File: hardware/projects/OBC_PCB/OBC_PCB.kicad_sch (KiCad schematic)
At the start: 40 parts, among them U6 nRF54LM20A-QGAA, Y1 32MHz, Y3 32.768kHz

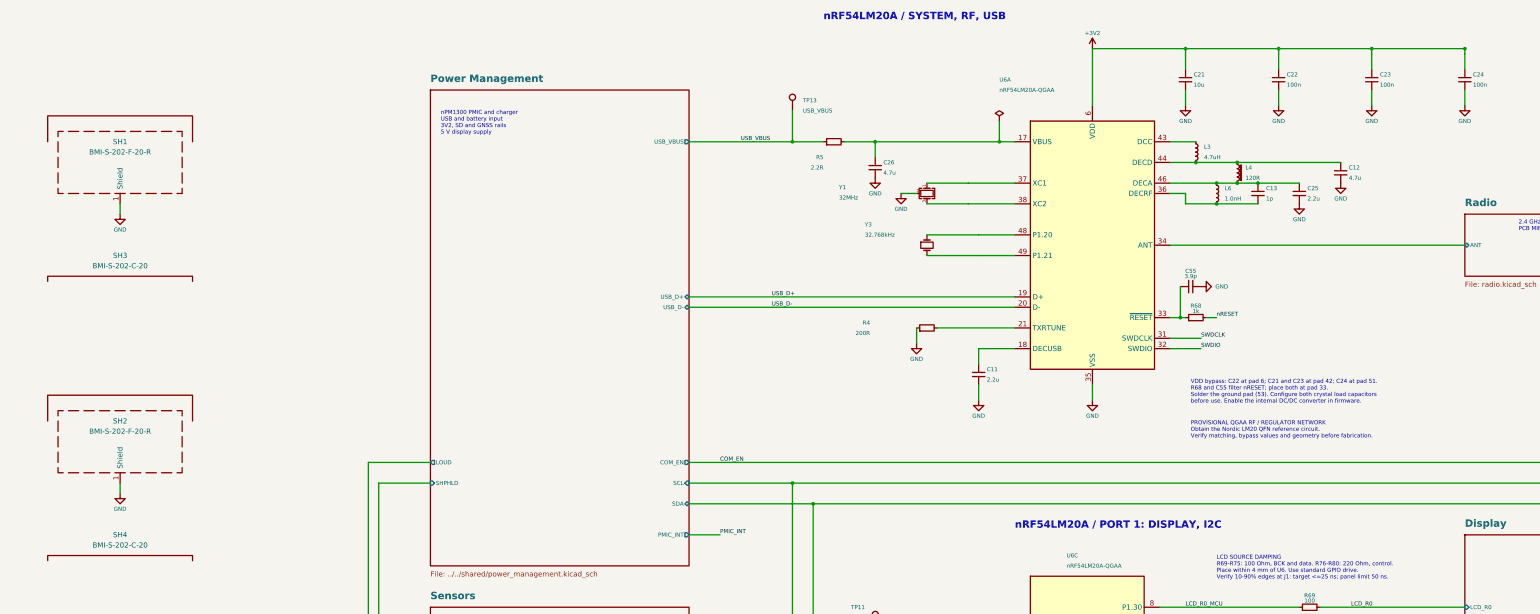
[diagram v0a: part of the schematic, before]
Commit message: hardware: save current KiCad schematic and project files
Retain the saved KiCad 10 schematic files and project sheet list.
The native netlist matches the committed placement circuit: 172
components and 140 nets. Public docs unchanged.
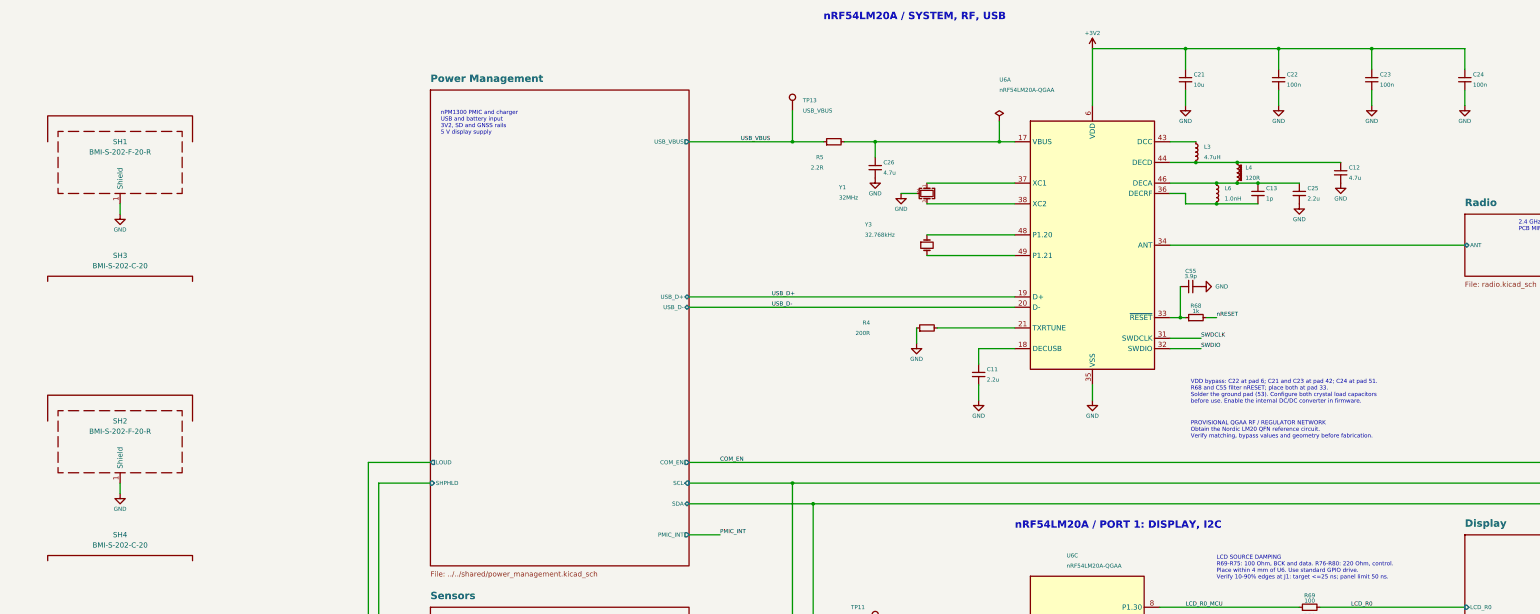
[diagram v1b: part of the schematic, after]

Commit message: hardware: add editable KiCad BOM and schematic exports
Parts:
- C11: DigiKey (none) -> https://www.digikey.de/en/products/detail/samsung-electro-m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; MPN (none) -> CL05A225KP5NNNC; Manufacturer (none) -> Samsung Electro-Mechanics; Mouser (none) -> https://www.mouser.com/en/ProductDetail/Samsung-Electro-Mec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; Price breaks EUR (none) -> 1:0.12000;10:0.06700;50:0.04740;100:0.04110;500:0.03058;100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; Price checked (none) -> 2026-10-02; Price source (none) -> https://www.digikey.de/en/products/detail/samsung-electro-m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; Sourcing notes (none) -> Mouser shows limited stock; DigiKey EUR price used.
- C12: Mouser (none) -> https://eu.mouser.com/en/ProductDetail/Murata-Electronics/G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; Price breaks EUR (none) -> 1:0.206;10:0.127;100:0.077;500:0.06;1000:0.054;2500:0.048;5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; Price checked (none) -> 2026-10-02; Price source (none) -> https://eu.mouser.com/en/ProductDetail/Murata-Electronics/G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
- C13: Mouser (none) -> https://eu.mouser.com/en/ProductDetail/Murata-Electronics/G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; Price breaks EUR (none) -> 1:0.086;10:0.034;100:0.028;500:0.022;1000:0.019;2500:0.017;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; Price checked (none) -> 2026-10-02; Price source (none) -> https://eu.mouser.com/en/ProductDetail/Murata-Electronics/G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
- C21: MPN (none) -> CC0402MRX6S5BB106; Manufacturer (none) -> YAGEO; Mouser (none) -> https://www.mouser.es/es/ProductDetail/YAGEO/CC0402MRX6S5BB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; Price breaks EUR (none) -> 1:0.542;10:0.294;100:0.217;500:0.174; Price checked (none) -> 2026-10-02; Price source (none) -> https://www.mouser.es/es/ProductDetail/YAGEO/CC0402MRX6S5BB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
- C22, C23, C24: DigiKey (none) -> https://www.digikey.de/en/products/detail/murata-electronic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; MPN (none) -> GRM155R71A104KA01D; Manufacturer (none) -> Murata; Price breaks EUR (none) -> 1:0.09000;10:0.02100;50:0.01400;100:0.01190;500:0.00830; Price checked (none) -> 2026-10-02; Price source (none) -> https://www.digikey.de/en/products/detail/murata-electronic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
- C25: Mouser (none) -> https://hr.mouser.com/en/ProductDetail/Murata-Electronics/G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; Price breaks EUR (none) -> 1:0.103;10:0.04;100:0.035;500:0.026;1000:0.024;2500:0.022;5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; Price checked (none) -> 2026-10-02; Price source (none) -> https://hr.mouser.com/en/ProductDetail/Murata-Electronics/G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
- C26: Mouser (none) -> https://gr.mouser.com/en/ProductDetail/Murata-Electronics/G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; Price breaks EUR (none) -> 1:0.146;10:0.061;100:0.035;500:0.028;1000:0.022;2500:0.02;5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; Price checked (none) -> 2026-10-02; Price source (none) -> https://gr.mouser.com/en/ProductDetail/Murata-Electronics/G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
- C55: MPN (none) -> GJM0335C1E3R9BB01D; Manufacturer (none) -> Murata; Mouser (none) -> https://www.mouser.fr/ProductDetail/Murata-Electronics/GJM0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; Price breaks EUR (none) -> 1:0.086;10:0.023;100:0.021;500:0.015; Price checked (none) -> 2026-10-02; Price source (none) -> https://www.mouser.fr/ProductDetail/Murata-Electronics/GJM0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
- L3: DigiKey (none) -> https://www.digikey.de/en/products/detail/tdk/MLZ1608M4R7WT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; Mouser (none) -> https://eu.mouser.com/en/ProductDetail/TDK/MLZ1608M4R7WT000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; Price breaks EUR (none) -> 1:0.09000;10:0.07400;100:0.06040;1000:0.04959; Price checked (none) -> 2026-10-02; Price source (none) -> https://www.digikey.de/en/products/detail/tdk/MLZ1608M4R7WT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
- L4: Mouser (none) -> https://www.mouser.sk/en/ProductDetail/Murata-Electronics/B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; Price breaks EUR (none) -> 1:0.086;10:0.022;25:0.018;100:0.015;250:0.014;500:0.012;100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; Price checked (none) -> 2026-10-02; Price source (none) -> https://www.mouser.sk/en/ProductDetail/Murata-Electronics/B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
- L6: Mouser (none) -> https://www.mouser.es/ProductDetail/Murata-Electronics/LQP0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; Price breaks EUR (none) -> 1:0.086;10:0.022;100:0.018;1000:0.015;5000:0.011; Price checked (none) -> 2026-10-02; Price source (none) -> https://www.mouser.es/ProductDetail/Murata-Electronics/LQP0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
- R4: MPN (none) -> RC0402FR-07200RL; Manufacturer (none) -> YAGEO; Mouser (none) -> https://www.mouser.de/de/ProductDetail/YAGEO/RC0402FR-07200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; Power 63mW -> 62.5mW; Price breaks EUR (none) -> 1:0.086;10:0.008;100:0.005;2500:0.003; Price checked (none) -> 2026-10-02; Price source (none) -> https://www.mouser.de/de/ProductDetail/YAGEO/RC0402FR-07200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
- R5: DigiKey (none) -> https://www.digikey.fr/fr/products/detail/yageo/RC0402FR-07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; MPN (none) -> RC0402FR-072R2L; Manufacturer (none) -> YAGEO; Mouser (none) -> https://www.mouser.com/en/ProductDetail/YAGEO/RC0402FR-072R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; Power 63mW -> 62.5mW; Price breaks EUR (none) -> 1:0.09;10:0.021;25:0.0152;50:0.0122;100:0.0099;250:0.0076;5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; Price checked (none) -> 2026-10-02; Price source (none) -> https://www.digikey.fr/fr/products/detail/yageo/RC0402FR-07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; Technology (none) -> Thick film
- R68: DigiKey (none) -> https://www.digikey.de/de/products/detail/yageo/RC0201FR-07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; MPN (none) -> RC0201FR-071KL; Manufacturer (none) -> YAGEO; Mouser (none) -> https://gr.mouser.com/en/ProductDetail/YAGEO/RC0201FR-071KL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; Power 63mW -> 50mW; Price breaks EUR (none) -> 1:0.172;10:0.017;100:0.011;1000:0.009; Price checked (none) -> 2026-10-02; Price source (none) -> https://gr.mouser.com/en/ProductDetail/YAGEO/RC0201FR-071KL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; Selection notes (none) -> Candidate; verify the 0201 part rating of 50mW/25V against 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; Voltage 50V -> 25V
- R69, R70, R71, R72, R73, R74, R75: Mouser (none) -> https://eu.mouser.com/ProductDetail/YAGEO/RC0201FR-07100RL?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; Price breaks EUR (none) -> 1:0.086;10:0.008;100:0.006;1000:0.005; Price checked (none) -> 2026-10-02; Price source (none) -> https://eu.mouser.com/ProductDetail/YAGEO/RC0201FR-07100RL?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
- R76, R77, R78, R79, R80: Mouser (none) -> https://eu.mouser.com/en/ProductDetail/YAGEO/RC0201FR-07220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; Price breaks EUR (none) -> 1:0.086;10:0.009;100:0.007;1000:0.005; Price checked (none) -> 2026-10-02; Price source (none) -> https://eu.mouser.com/en/ProductDetail/YAGEO/RC0201FR-07220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
- R9: MPN (none) -> RC0402FR-0733RL; Manufacturer (none) -> YAGEO; Mouser (none) -> https://eu.mouser.com/en/ProductDetail/YAGEO/RC0402FR-0733R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; Power 63mW -> 62.5mW; Price breaks EUR (none) -> 1:0.086;10:0.009;100:0.006;1000:0.005;2500:0.003; Price checked (none) -> 2026-10-02; Price source (none) -> https://eu.mouser.com/en/ProductDetail/YAGEO/RC0402FR-0733R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
- SH1, SH2: DigiKey (none) -> https://www.digikey.ie/en/products/detail/laird-technologie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; Price breaks EUR (none) -> 1:1.70000;10:1.46300;25:1.38160;100:1.26850;250:1.20076; Price checked (none) -> 2026-10-02; Price source (none) -> https://www.digikey.ie/en/products/detail/laird-technologie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
- SH3, SH4: Mouser (none) -> https://eu.mouser.com/ProductDetail/Laird-Technologies/BMI-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; Price breaks EUR (none) -> 1:1.38;10:1.01;25:0.92;100:0.818;250:0.77;500:0.74;900:0.71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; Price checked (none) -> 2026-10-02; Price source (none) -> https://eu.mouser.com/ProductDetail/Laird-Technologies/BMI-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
- U6: Alternate MPN (none) -> NRF54LM20A-QGAA-R7; Alternate source (none) -> https://www.digikey.de/de/products/detail/nordic-semiconduc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; MPN nRF54LM20A-QGAA-R7 -> NRF54LM20A-QGAA-R; Mouser (none) -> https://eu.mouser.com/en/ProductDetail/Nordic-Semiconductor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; Price breaks EUR (none) -> 1:4.57;10:3.48;25:3.21;100:2.91;250:2.89; Price checked (none) -> 2026-10-02; Price source (none) -> https://eu.mouser.com/en/ProductDetail/Nordic-Semiconductor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; Sourcing notes (none) -> Backorder: Mouser shows 2935 expected 2027-01-20. Estimate,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
- Y1: DigiKey (none) -> https://www.digikey.de/de/products/detail/kyocera-avx/CX201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; Mouser (none) -> https://www.mouser.com/ProductDetail/KYOCERA-AVX/CX2016DB32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; Price breaks EUR (none) -> 1:0.75000;10:0.65400;25:0.61800;50:0.59240;100:0.56790;250: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; Price checked (none) -> 2026-10-02; Price source (none) -> https://www.digikey.de/de/products/detail/kyocera-avx/CX201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
- Y3: Mouser (none) -> https://eu.mouser.com/en/ProductDetail/TXC-Corporation/9HT1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; Price breaks EUR (none) -> 1:0.705;10:0.614;25:0.556;100:0.534;250:0.505;500:0.484;100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; Price checked (none) -> 2026-10-02; Price source (none) -> https://eu.mouser.com/en/ProductDetail/TXC-Corporation/9HT1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
